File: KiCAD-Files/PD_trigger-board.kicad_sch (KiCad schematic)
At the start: 16 parts, among them J1 USB_C_Receptacle_USB3.0_12P, U1 HUSB238, U2 SI4459ADY-T1-GE3, U3 ESP32-S3-mini_pinprofile

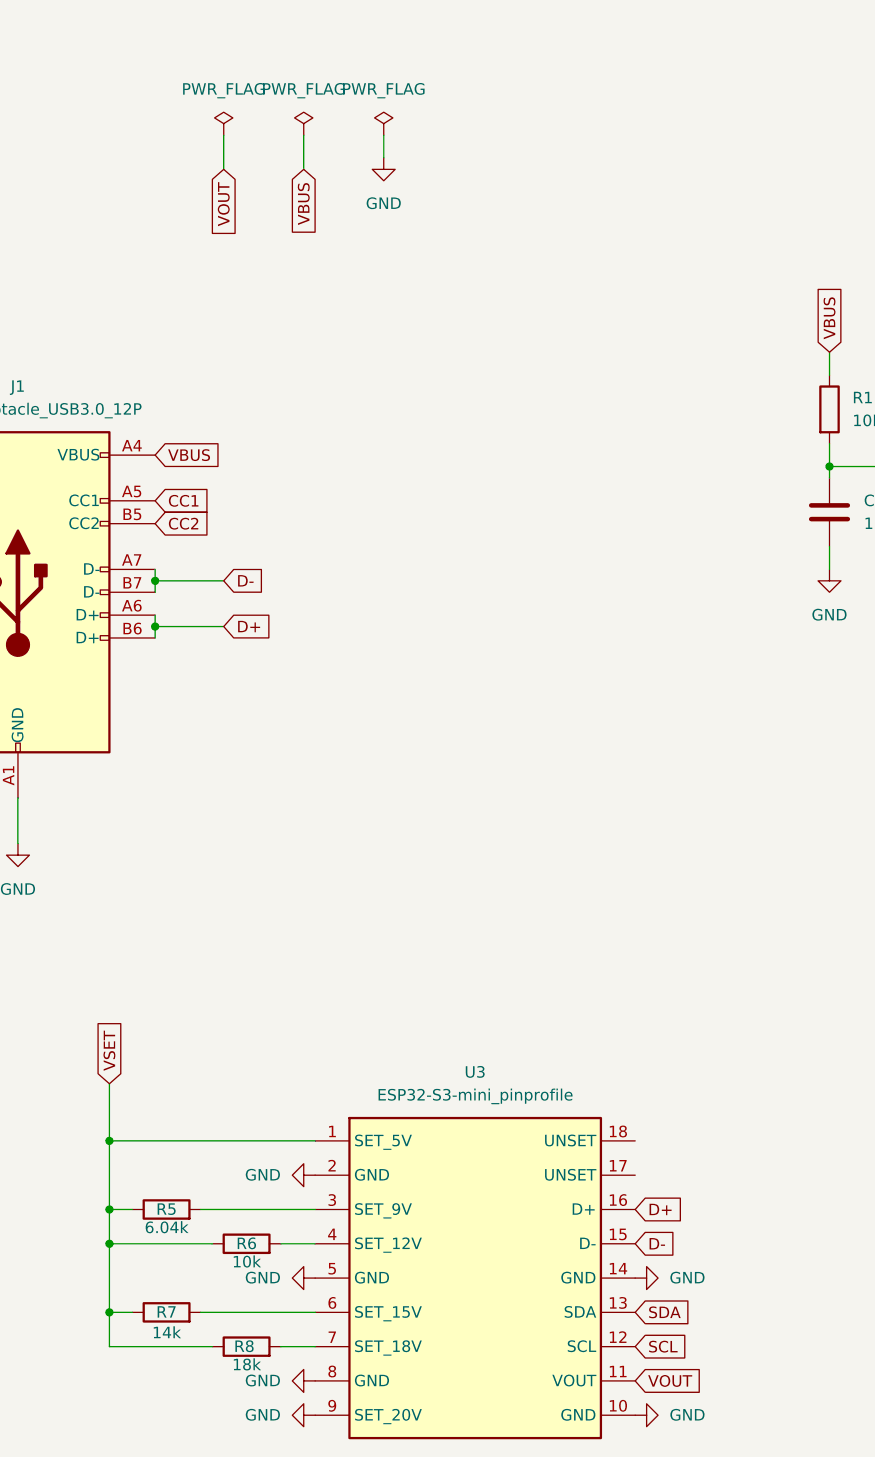
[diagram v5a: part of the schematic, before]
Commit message: Layout completed, ToDo processed
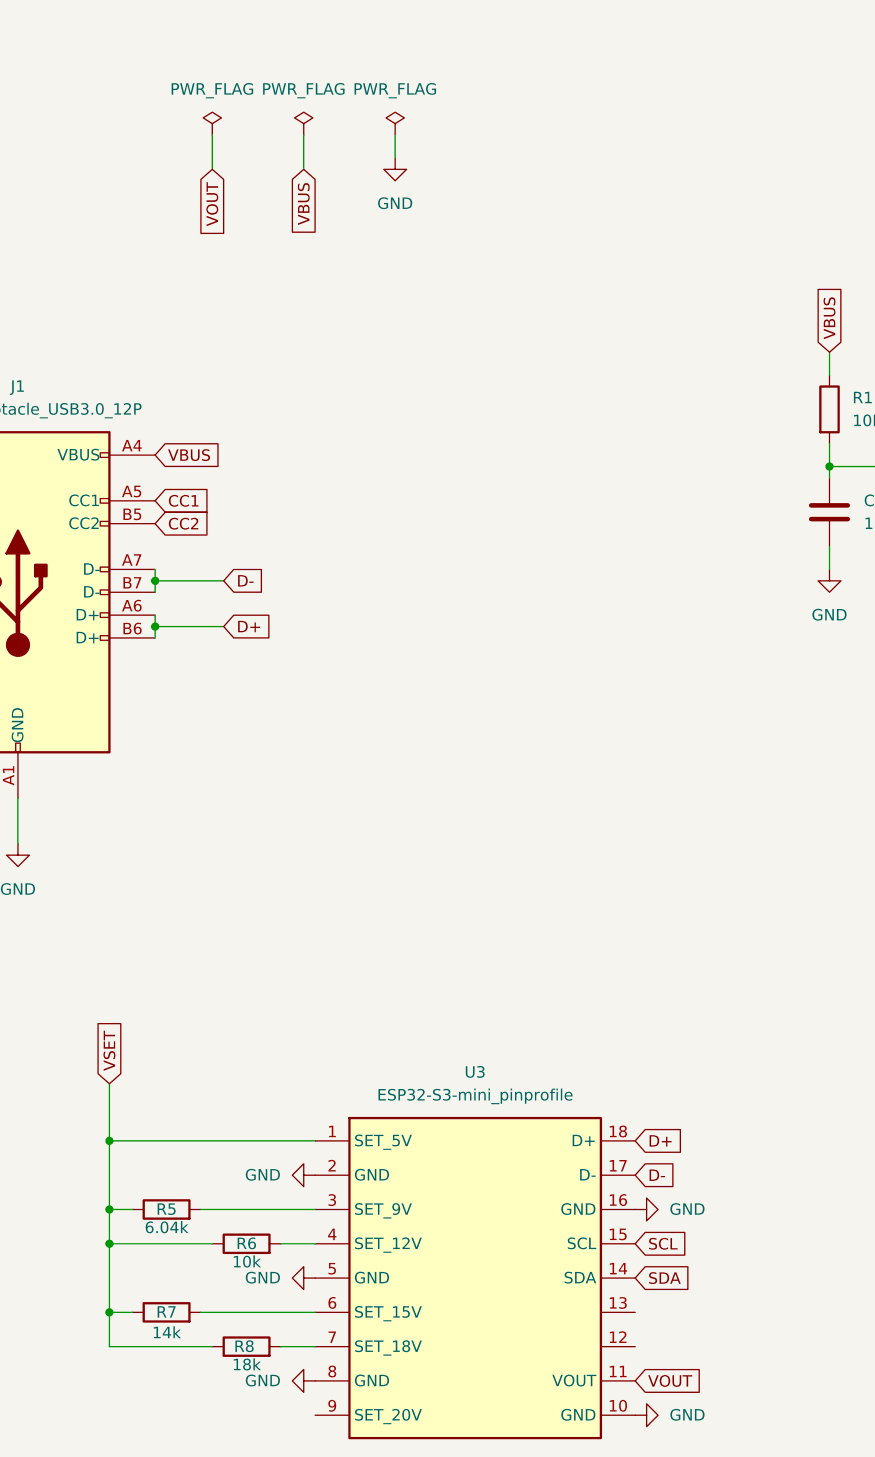
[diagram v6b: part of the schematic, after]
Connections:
- net D+: now also U3.18 (D+); no longer U3.16 (D+)
- net D-: now also U3.17 (D-); no longer U3.15 (D-)
- net GND: now also U3.16 (GND); no longer U3.14 (GND), U3.9 (SET_20V)
- net SCL: now also U3.15 (SCL); no longer U3.12 (SCL)
- net SDA: now also U3.14 (SDA); no longer U3.13 (SDA)
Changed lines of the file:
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@@
 	(wire
 		(pts
-			(xy 254 35.56) (xy 264.16 35.56)
+			(xy 220.98 30.48) (xy 220.98 33.02)
 		)
 		(stroke
@@
 	(wire
 		(pts
-			(xy 146.05 71.12) (xy 130.81 71.12)
+			(xy 254 35.56) (xy 264.16 35.56)
 		)
 		(stroke
@@
 	(wire
 		(pts
-			(xy 146.05 81.28) (xy 146.05 71.12)
+			(xy 146.05 71.12) (xy 130.81 71.12)
 		)
 		(stroke
@@
 	(wire
 		(pts
-			(xy 236.22 30.48) (xy 236.22 33.02)
+			(xy 146.05 81.28) (xy 146.05 71.12)
 		)
 		(stroke
@@
 	(wire
 		(pts
-			(xy 236.22 33.02) (xy 236.22 35.56)
+			(xy 236.22 30.48) (xy 236.22 33.02)
 		)
 		(stroke
@@
 	(wire
 		(pts
-			(xy 40.64 107.95) (xy 40.64 113.03)
+			(xy 236.22 33.02) (xy 236.22 35.56)
 		)
 		(stroke
@@
 	(wire
 		(pts
-			(xy 220.98 30.48) (xy 220.98 33.02)
+			(xy 40.64 107.95) (xy 40.64 113.03)
 		)
 		(stroke
@@
 	(wire
 		(pts
-			(xy 81.28 34.29) (xy 81.28 36.83)
+			(xy 82.55 34.29) (xy 82.55 36.83)
 		)
 		(stroke
@@
 	(wire
 		(pts
-			(xy 63.5 34.29) (xy 63.5 38.1)
+			(xy 62.23 34.29) (xy 62.23 38.1)
 		)
 		(stroke
@@
 	(global_label "VOUT"
 		(shape input)
-		(at 63.5 38.1 270)
+		(at 62.23 38.1 270)
 		(fields_autoplaced yes)
 		(effects
@@
 		)
 		(property "Intersheetrefs" "${INTERSHEET_REFS}"
-			(at 63.5 45.8024 90)
+			(at 62.23 45.8024 90)
 			(effects
 				(font
@@
 	(global_label "SCL"
 		(shape input)
-		(at 109.22 168.91 0)
+		(at 109.22 157.48 0)
 		(fields_autoplaced yes)
 		(effects
@@
 		)
 		(property "Intersheetrefs" "${INTERSHEET_REFS}"
-			(at 115.7128 168.91 0)
+			(at 115.7128 157.48 0)
 			(effects
 				(font
@@
 	(global_label "D-"
 		(shape input)
-		(at 109.22 157.48 0)
+		(at 109.22 149.86 0)
 		(fields_autoplaced yes)
 		(effects
@@
 		)
 		(property "Intersheetrefs" "${INTERSHEET_REFS}"
-			(at 115.0476 157.48 0)
+			(at 115.0476 149.86 0)
 			(effects
 				(font
@@
 	(global_label "SDA"
 		(shape input)
-		(at 109.22 165.1 0)
+		(at 109.22 161.29 0)
 		(fields_autoplaced yes)
 		(effects
@@
 		)
 		(property "Intersheetrefs" "${INTERSHEET_REFS}"
-			(at 115.7733 165.1 0)
+			(at 115.7733 161.29 0)
 			(effects
 				(font
@@
 	(global_label "D+"
 		(shape input)
-		(at 109.22 153.67 0)
+		(at 109.22 146.05 0)
 		(fields_autoplaced yes)
 		(effects
@@
 		)
 		(property "Intersheetrefs" "${INTERSHEET_REFS}"
-			(at 115.0476 153.67 0)
+			(at 115.0476 146.05 0)
 			(effects
 				(font
@@
 	(symbol
 		(lib_id "power:GND")
-		(at 81.28 36.83 0)
+		(at 82.55 36.83 0)
 		(unit 1)
 		(exclude_from_sim no)
@@
 		(fields_autoplaced yes)
 		(property "Reference" "#PWR03"
-			(at 81.28 43.18 0)
+			(at 82.55 43.18 0)
 			(effects
 				(font
@@
 		)
 		(property "Value" "GND"
-			(at 81.28 41.91 0)
+			(at 82.55 41.91 0)
 			(effects
 				(font
@@
 		)
 		(property "Footprint" ""
-			(at 81.28 36.83 0)
+			(at 82.55 36.83 0)
 			(effects
 				(font
@@
 		)
 		(property "Datasheet" ""
-			(at 81.28 36.83 0)
+			(at 82.55 36.83 0)
 			(effects
 				(font
@@
 		)
 		(property "Description" "Power symbol creates a global label with name \"GND\" , ground"
-			(at 81.28 36.83 0)
+			(at 82.55 36.83 0)
 			(effects
 				(font
@@
 		(on_board yes)
 		(dnp no)
-		(fields_autoplaced yes)
 		(property "Reference" "#FLG02"
 			(at 72.39 32.385 0)
@@
 	(symbol
 		(lib_id "power:PWR_FLAG")
-		(at 63.5 34.29 0)
+		(at 62.23 34.29 0)
 		(unit 1)
 		(exclude_from_sim no)
@@
 		(fields_autoplaced yes)
 		(property "Reference" "#FLG01"
-			(at 63.5 32.385 0)
+			(at 62.23 32.385 0)
 			(effects
 				(font
@@
 		)
 		(property "Value" "PWR_FLAG"
-			(at 63.5 29.21 0)
+			(at 62.23 29.21 0)
 			(effects
 				(font
@@
 		)
 		(property "Footprint" ""
-			(at 63.5 34.29 0)
+			(at 62.23 34.29 0)
 			(effects
 				(font
@@
 		)
 		(property "Datasheet" "~"
-			(at 63.5 34.29 0)
+			(at 62.23 34.29 0)
 			(effects
 				(font
@@
 		)
 		(property "Description" "Special symbol for telling ERC where power comes from"
-			(at 63.5 34.29 0)
+			(at 62.23 34.29 0)
 			(effects
 				(font
@@
 	(symbol
 		(lib_id "power:GND")
-		(at 73.66 176.53 270)
-		(unit 1)
-		(exclude_from_sim no)
-		(in_bom yes)
-		(on_board yes)
-		(dnp no)
-		(fields_autoplaced yes)
-		(property "Reference" "#PWR05"
-			(at 67.31 176.53 0)
-			(effects
-				(font
-					(size 1.27 1.27)
-				)
-				(hide yes)
-			)
-		)
-		(property "Value" "GND"
-			(at 69.85 176.5299 90)
-			(effects
-				(font
-					(size 1.27 1.27)
-				)
-				(justify right)
-			)
-		)
-		(property "Footprint" ""
-			(at 73.66 176.53 0)
-			(effects
-				(font
-					(size 1.27 1.27)
-				)
-				(hide yes)
-			)
-		)
-		(property "Datasheet" ""
-			(at 73.66 176.53 0)
-			(effects
-				(font
-					(size 1.27 1.27)
-				)
-				(hide yes)
-			)
-		)
-		(property "Description" "Power symbol creates a global label with name \"GND\" , ground"
-			(at 73.66 176.53 0)
-			(effects
-				(font
-					(size 1.27 1.27)
-				)
-				(hide yes)
-			)
-		)
-		(pin "1"
-		)
-		(instances
-			(project "PD_trigger-board"
-				(path "/e428d426-38f9-47e3-9715-a18ed772a1ec"
-					(reference "#PWR05")
-					(unit 1)
-				)
-			)
-		)
-	)
-	(symbol
-		(lib_id "power:GND")
 		(at 109.22 176.53 90)
 		(unit 1)
@@
 	(symbol
 		(lib_id "power:PWR_FLAG")
-		(at 81.28 34.29 0)
+		(at 82.55 34.29 0)
 		(unit 1)
 		(exclude_from_sim no)
@@
 		(fields_autoplaced yes)
 		(property "Reference" "#FLG03"
-			(at 81.28 32.385 0)
+			(at 82.55 32.385 0)
 			(effects
 				(font
@@
 		)
 		(property "Value" "PWR_FLAG"
-			(at 81.28 29.21 0)
+			(at 82.55 29.21 0)
 			(effects
 				(font
@@
 		)
 		(property "Footprint" ""
-			(at 81.28 34.29 0)
+			(at 82.55 34.29 0)
 			(effects
 				(font
@@
 		)
 		(property "Datasheet" "~"
-			(at 81.28 34.29 0)
+			(at 82.55 34.29 0)
 			(effects
 				(font
@@
 		)
 		(property "Description" "Special symbol for telling ERC where power comes from"
-			(at 81.28 34.29 0)
+			(at 82.55 34.29 0)
 			(effects
 				(font
@@
 	(symbol
 		(lib_id "power:GND")
-		(at 109.22 161.29 90)
+		(at 109.22 153.67 90)
 		(unit 1)
 		(exclude_from_sim no)
@@
 		(fields_autoplaced yes)
 		(property "Reference" "#PWR08"
-			(at 115.57 161.29 0)
+			(at 115.57 153.67 0)
 			(effects
 				(font
@@
 		)
 		(property "Value" "GND"
-			(at 113.03 161.2899 90)
+			(at 113.03 153.6699 90)
 			(effects
 				(font
@@
 		)
 		(property "Footprint" ""
-			(at 109.22 161.29 0)
+			(at 109.22 153.67 0)
 			(effects
 				(font
@@
 		)
 		(property "Datasheet" ""
-			(at 109.22 161.29 0)
+			(at 109.22 153.67 0)
 			(effects
 				(font
@@
 		)
 		(property "Description" "Power symbol creates a global label with name \"GND\" , ground"
-			(at 109.22 161.29 0)
+			(at 109.22 153.67 0)
 			(effects
 				(font

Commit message: Partdescription updated
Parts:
- C1: FCSC C15849 -> (none); LCSC (none) -> C15849
- C2, C3, C4: FCSC C307467 -> (none); LCSC (none) -> C307467
- J1: FCSC C136423 -> (none); LCSC (none) -> C136423
- R1: FCSC C25139 -> (none); LCSC (none) -> C25139
- R3: FCSC C100457 -> (none); LCSC (none) -> C100457
- R4: FCSC C25941 -> (none); LCSC (none) -> C25941
- R5: FCSC C25913 -> (none); LCSC (none) -> C25913
- R6: FCSC C25531 -> (none); LCSC (none) -> C25531
- R7, R9: FCSC C54831 -> (none); LCSC (none) -> C54831
- R8: FCSC C25542 -> (none); LCSC (none) -> C25542
- U1: FCSC C7471904 -> (none); LCSC (none) -> C7471904
- U2: FCSC C143743 -> (none); LCSC (none) -> C143743
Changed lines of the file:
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@@
 			)
 		)
-		(property "FCSC" "C307467"
+		(property "LCSC" "C307467"
 			(at 254 39.37 0)
 			(effects
@@
 			)
 		)
-		(property "FCSC" "C25941"
+		(property "LCSC" "C25941"
 			(at 226.06 52.07 0)
 			(effects
@@
 			)
 		)
-		(property "FCSC" "C100457"
+		(property "LCSC" "C100457"
 			(at 214.63 41.91 0)
 			(effects
@@
 			)
 		)
-		(property "FCSC" "C25913"
+		(property "LCSC" "C25913"
 			(at 57.15 153.67 90)
 			(effects
@@
 			)
 		)
-		(property "FCSC" "C25531"
+		(property "LCSC" "C25531"
 			(at 66.04 157.48 90)
 			(effects
@@
 			)
 		)
-		(property "FCSC" "C307467"
+		(property "LCSC" "C307467"
 			(at 243.84 39.37 0)
 			(effects
@@
 			)
 		)
-		(property "FCSC" "C136423"
+		(property "LCSC" "C136423"
 			(at 40.64 85.09 0)
 			(effects
@@
 			)
 		)
-		(property "FCSC" "C54831"
+		(property "LCSC" "C54831"
 			(at 193.04 100.33 90)
 			(effects
@@
 			)
 		)
-		(property "FCSC" "C143743"
+		(property "LCSC" "C143743"
 			(at 226.06 40.64 90)
 			(effects
@@
 			)
 		)
-		(property "FCSC" "C54831"
+		(property "LCSC" "C54831"
 			(at 57.15 165.1 90)
 			(effects
@@
 			)
 		)
-		(property "FCSC" "C7471904"
+		(property "LCSC" "C7471904"
 			(at 170.18 88.9 0)
 			(effects
@@
 			)
 		)
-		(property "FCSC" "C307467"
+		(property "LCSC" "C307467"
 			(at 264.16 39.37 0)
 			(effects
@@
 			)
 		)
-		(property "FCSC" "C15849"
+		(property "LCSC" "C15849"
 			(at 130.81 76.2 0)
 			(effects
@@
 			)
 		)
-		(property "FCSC" "C25139"
+		(property "LCSC" "C25139"
 			(at 130.81 64.77 0)
 			(effects
@@
 			)
 		)
-		(property "FCSC" "C25542"
+		(property "LCSC" "C25542"
 			(at 66.04 168.91 90)
 			(effects

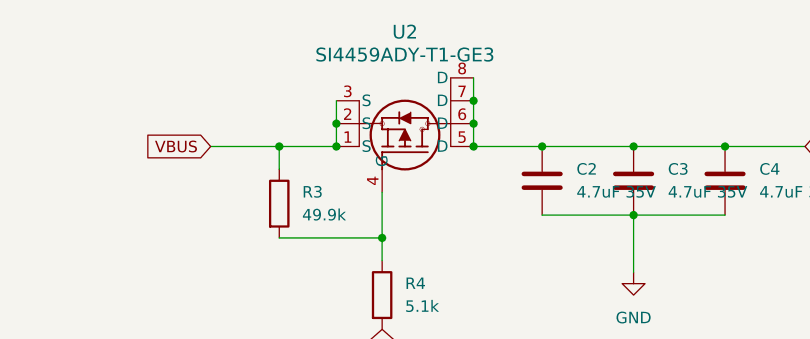
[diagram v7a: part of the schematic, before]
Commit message: MOSFET changed to SIR1309DP
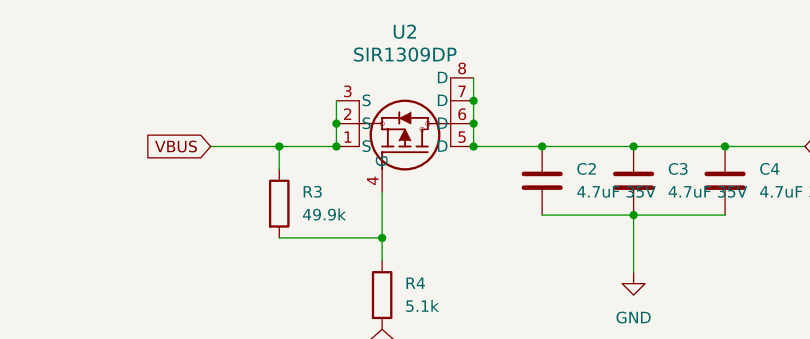
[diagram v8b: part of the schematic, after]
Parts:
- U2: value SI4459ADY-T1-GE3 -> SIR1309DP; LCSC C143743 -> C5919282
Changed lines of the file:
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@@
 			)
 		)
-		(property "Value" "SI4459ADY-T1-GE3"
+		(property "Value" "SIR1309DP"
 			(at 228.6 25.4 90)
 			(effects
@@
 			)
 		)
-		(property "LCSC" "C143743"
+		(property "LCSC" "C5919282"
 			(at 226.06 40.64 90)
 			(effects
